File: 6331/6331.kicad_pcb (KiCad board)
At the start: 2 copper layers, 21.6 x 34.3 mm, 3 parts, among them U1 ATF22V10C-10PU

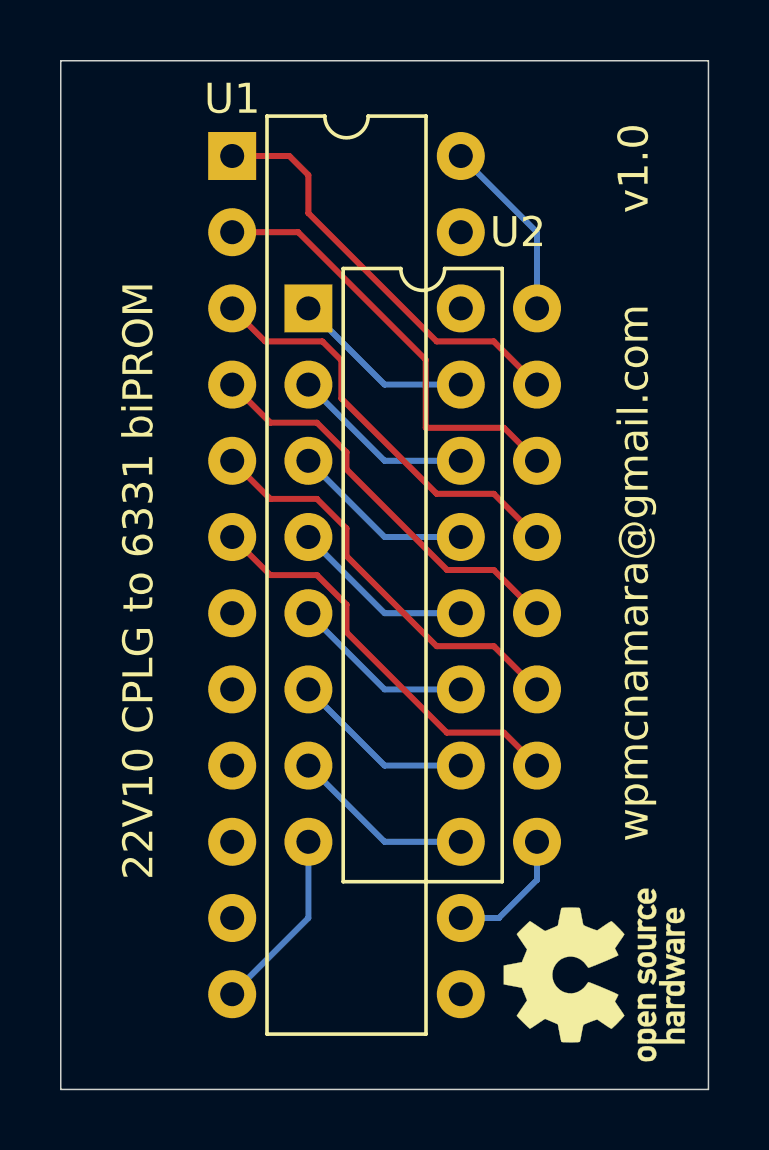
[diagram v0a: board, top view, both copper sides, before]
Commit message: PCB update to fix power trace widths and add board rev
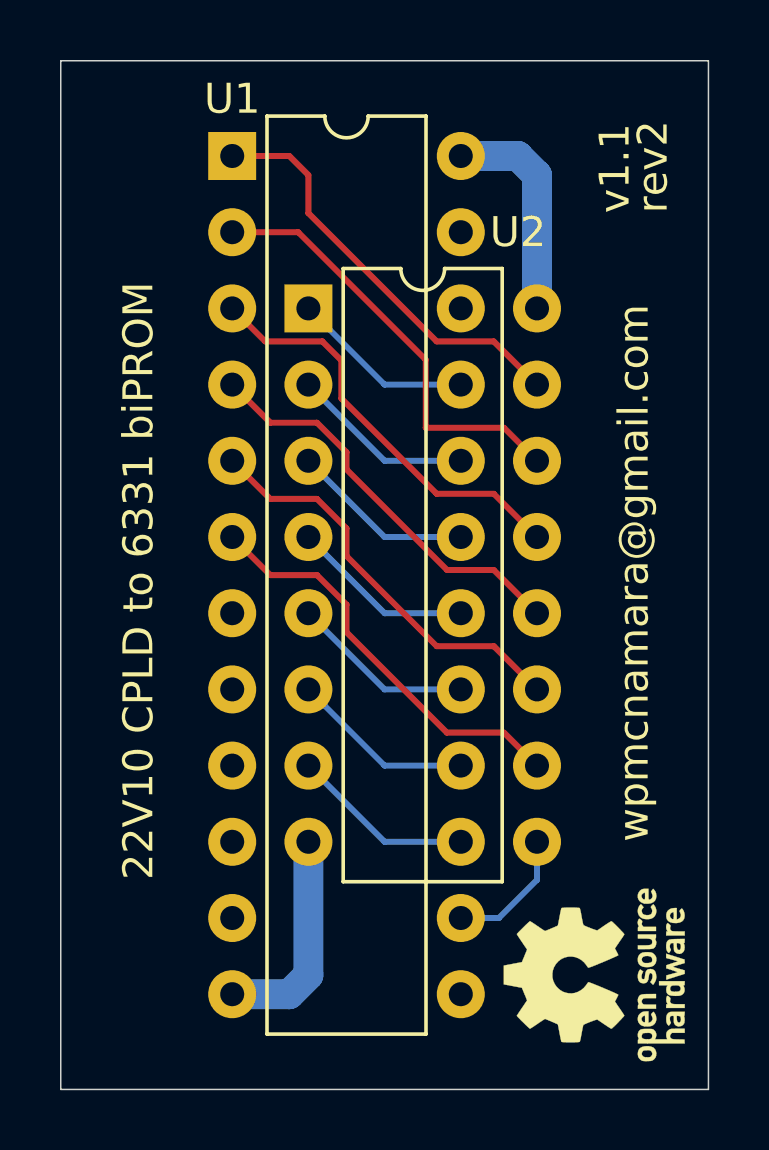
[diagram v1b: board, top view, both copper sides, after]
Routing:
- net Net-(U1-GND): track 6.13 -> 7.25 mm
- net Net-(U1-VCC): track 6.13 -> 7.25 mm
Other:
- board text added: "22V10 CPLD to 6331 biPROM"
- board text added: "rev2"
- board text added: "v1.1"
- board text removed: "22V10 CPLG to 6331 biPROM"
- board text removed: "v1.0"
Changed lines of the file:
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@@
 		(layer "Edge.Cuts")
 	)
-	(gr_text "v1.0"
-		(at 214.63 -452.755 90)
+	(gr_text "v1.1"
+		(at 213.995 -452.755 90)
 		(layer "F.SilkS")
 		(effects
@@
 		)
 	)
-	(gr_text "22V10 CPLG to 6331 biPROM"
+	(gr_text "22V10 CPLD to 6331 biPROM"
 		(at 198.12 -430.53 90)
+		(layer "F.SilkS")
+		(effects
+			(font
+				(size 1 1)
+				(thickness 0.1)
+			)
+			(justify left bottom)
+		)
+	)
+	(gr_text "rev2"
+		(at 215.265 -452.755 90)
 		(layer "F.SilkS")
 		(effects
@@
 	)
 	(segment
-		(start 210.82 -449.58)
-		(end 210.82 -452.12)
-		(width 0.2)
+		(start 210.82 -454.025)
+		(end 210.185 -454.66)
+		(width 1)
 		(layer "B.Cu")
 		(net 1)
 	)
 	(segment
-		(start 210.82 -452.12)
+		(start 210.185 -454.66)
 		(end 208.28 -454.66)
-		(width 0.2)
+		(width 1)
 		(layer "B.Cu")
 		(net 1)
 	)
 	(segment
-		(start 200.66 -426.72)
-		(end 203.2 -429.26)
-		(width 0.2)
+		(start 210.82 -449.58)
+		(end 210.82 -454.025)
+		(width 1)
+		(layer "B.Cu")
+		(net 1)
+	)
+	(segment
+		(start 203.2 -427.355)
+		(end 202.565 -426.72)
+		(width 1)
 		(layer "B.Cu")
 		(net 2)
 	)
 	(segment
-		(start 203.2 -429.26)
-		(end 203.2 -431.8)
-		(width 0.2)
+		(start 203.2 -431.8)
+		(end 203.2 -427.355)
+		(width 1)
 		(layer "B.Cu")
 		(net 2)
+	)
+	(segment
+		(start 202.565 -426.72)
+		(end 200.66 -426.72)
+		(width 1)
+		(layer "B.Cu")
+		(net 2)

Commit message: Better layout of PCB to simplify construction.  V1.2 of design.
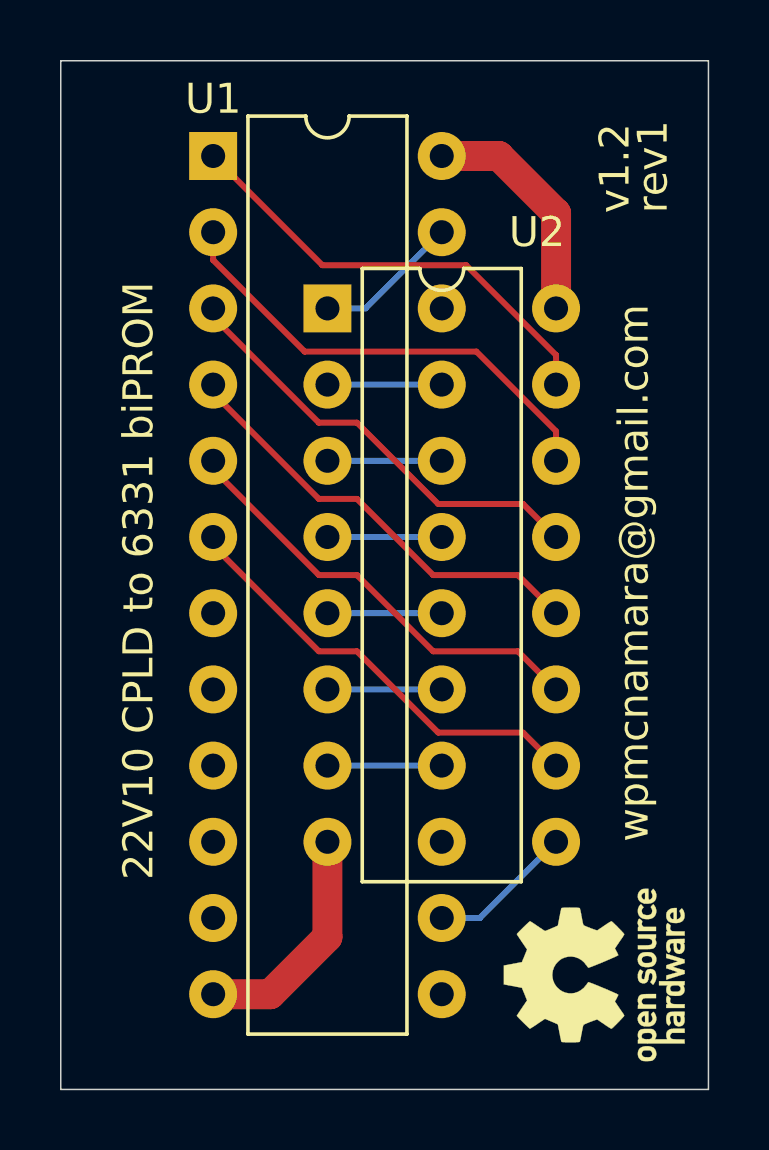
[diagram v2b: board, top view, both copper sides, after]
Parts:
- moved U2 0.64 mm to (203.8, -449.6)
- moved U1 0.63 mm to (200.0, -454.7)
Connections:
- U1 pad 15: Net-(U1-IO1) -> unconnected-(U1-IO1-Pad15)
- U1 pad 23: unconnected-(U1-IO9-Pad23) -> Net-(U1-IO9)
- U2 pad 1: Net-(U1-IO7) -> Net-(U1-IO9)
- U2 pad 2: Net-(U1-IO6) -> Net-(U1-IO7)
- U2 pad 3: Net-(U1-IO5) -> Net-(U1-IO6)
- U2 pad 4: Net-(U1-IO4) -> Net-(U1-IO5)
- U2 pad 5: Net-(U1-IO3) -> Net-(U1-IO4)
- U2 pad 6: Net-(U1-IO2) -> Net-(U1-IO3)
- U2 pad 7: Net-(U1-IO1) -> Net-(U1-IO2)
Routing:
- net Net-(U1-IO1): track 6.13 -> 0.00 mm
- net Net-(U1-IO9): track 0.00 -> 4.86 mm
- net Net-(U1-IO6): track 6.13 -> 3.81 mm
- net Net-(U1-IO5): track 6.13 -> 3.81 mm
- net Net-(U1-IO3): track 6.13 -> 3.81 mm
- net Net-(U1-IO2): track 6.13 -> 3.81 mm
- net Net-(U1-IO7): track 6.13 -> 3.81 mm
- net Net-(U1-IO4): track 6.13 -> 3.81 mm
- net Net-(U1-PD/IN3): track 13.7 -> 14.8 mm
- net Net-(U1-CLK/IN0): track 14.1 -> 15.2 mm
- net Net-(U1-IN1): track 14.6 -> 15.7 mm
- net Net-(U1-IN4): track 13.9 -> 14.8 mm
- net Net-(U1-IN5): track 13.9 -> 14.8 mm
- net Net-(U1-IN2): track 14.1 -> 14.8 mm
- net Net-(U1-VCC): track 7.25 -> 7.77 mm
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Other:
- board text added: "rev1"
- board text added: "v1.2"
- board text removed: "rev2"
- board text removed: "v1.1"
